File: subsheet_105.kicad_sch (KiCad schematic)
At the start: 0 parts

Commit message: prepare feuille circuit video
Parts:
- added B03: Sortie vidéo, symbol Connector_Generic:Conn_01x09
- added C? (x3): 47nF, symbol Device:C_Small
- added C?: 100uF, symbol Device:C_Polarized_Small
- added C?: 10nF, symbol Device:C_Small
- added D?: 1N4148, symbol Device:D_Small
- added I06, I10: 74LS173 Registre D 4 bits, Package_DIP:DIP-16_W7.62mm_LongPads, symbol 74x173:4-BIT_D-TYPE_REGISTERS_WITH_3-STATE_OUTPUTS_PHY
- added I18: 74LS165 Sérialiseur 8:1, Package_DIP:DIP-16_W7.62mm_LongPads, symbol 74x165:PARALLEL-LOAD_8-BIT_SHIFT_REGISTERS_PHY
- added I25: 74LS126 Quadruple tampon de bus, Package_DIP:DIP-14_W7.62mm_LongPads, symbol 74x126:QUADRUPLE_BUS_BUFFERS_WITH_3-STATE_OUTPUTS_PHY
- added R?: 22K, symbol Device:R_Small
- added R?: 3K3, symbol Device:R_Small
- added T01, T02, T03: BC547B, symbol Device:Q_NPN_EBC
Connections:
- new net +5V: C?.1, C?.2
- new net GND: C?.1, C?.2

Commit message: continue circuit vidéo
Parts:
- added C22, C26, C30, C32, C36: 47nF, symbol Device:C_Small
- added C59: 18pF, symbol Device:C_Small
- added D04, D05, D06: 1N4148, symbol Device:D_Small
- added I03: HM7603 32×8 PROM, Package_DIP:DIP-16_W7.62mm_LongPads, symbol hm7603:HM7603_32×8_PROM_THREE-STATE_OUTPUTS_PHY
- added R01, R03, R05: 1K, symbol Device:R_Small
- added R02, R04, R06: 68, symbol Device:R_Small
- added R14, R17, R20: 10K, symbol Device:R_Small
- added R15, R18, R21: 3K, symbol Device:R_Small
- added R16, R19, R22: 22K, symbol Device:R_Small
- added R23, R24, R25, R26, R27, R28: 4K7, symbol Device:R_Small
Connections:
- net +5V: now also I06.16 (VCC), I10.16 (VCC), I18.16 (VCC), I25.14 (VCC), T01.3 (C), T02.3 (C), T03.3 (C), C22.1, C26.1, C30.1, C32.1, C36.2, I03.16 (VCC), R23.1, R24.1, R25.1, R26.1, R27.1, R28.1
- net GND: now also B03.6 (Pin_6), I06.10 (~{G2}), I06.15 (CLR), I06.8 (GND), I06.9 (~{G1}), I10.10 (~{G2}), I10.15 (CLR), I10.8 (GND), I10.9 (~{G1}), I18.15 (CLK_INH), I25.7 (GND), C22.2, C26.2, C30.2, C32.2, C36.1, I03.15 (~{CE}), I03.8 (GND), R01.2, R03.2, R05.2, R14.2, R17.2, R20.2
- net at T01.1 (E): now also R01.1, R02.2
- net at T01.2 (B): now also R14.1, R15.1, R16.1
- net ~{INILT}: now reaches I25.1 (1G)
- net ~{INILT}: now also I06.2 (~{OE2}), I10.2 (~{OE2}), I25.10 (3G), I25.13 (4G), I25.4 (2G)
- net ROUGE: now reaches I25.11 (4Y)
- net ROUGE: now also I06.6 (4Q), I10.6 (4Q), I03.10 (A0)
- net RT: now reaches I25.12 (4A)
- net PT: now reaches I25.2 (1A)
- net PASTEL: now reaches I25.3 (1Y)
- net PASTEL: now also I06.3 (1Q), I10.3 (1Q), I03.13 (A3)
- net BT: now reaches I25.5 (2A)
- net BLEU: now reaches I25.6 (2Y)
- net BLEU: now also I06.4 (2Q), I10.4 (2Q), I03.12 (A2)
- net VERT: now reaches I25.8 (3Y)
- net VERT: now also I06.5 (3Q), I10.5 (3Q), I03.11 (A1)
- net VT: now reaches I25.9 (3A)
- net at I06.1 (~{OE1}): now also I18.7 (~{QH})
- net at T03.1 (E): now also R05.1, R06.2
- net at T03.2 (B): now also R20.1, R21.1, R22.1
- net at I18.9 (QH): now also I10.1 (~{OE1})
- net at T02.1 (E): now also R03.1, R04.2
- net at T02.2 (B): now also R17.1, R18.1, R19.1
- net N/SON TV: now reaches B03.1 (Pin_1)
- net B: now reaches B03.2 (Pin_2)
- net B: now also R02.1
- net R: now reaches B03.3 (Pin_3)
- net R: now also R06.1
- net CRTV: now reaches B03.4 (Pin_4)
- net F/VIDEO: now reaches B03.5 (Pin_5)
- net V: now reaches B03.7 (Pin_7)
- net V: now also R04.1
- net SYNTV: now reaches B03.8 (Pin_8)
- net CLTV: now reaches B03.9 (Pin_9)
- new net: I03.1 (O1), R22.2, R23.2
- new net: D04.2 (A), I03.2 (O2), R24.2
- new net: I03.3 (O3), R19.2, R25.2
- new net: C59.2, D05.2 (A), I03.4 (O4), R26.2
- new net: I03.5 (O5), R16.2, R27.2
- new net: D06.2 (A), I03.6 (O6), R28.2
- new net: C59.1, D05.1 (K), R18.2
- new net: D04.1 (K), R21.2
- new net: D06.1 (K), R15.2
- new net ~{NOIR_INCR}: I03.9 (O8)
- new net ~{SUPLT}: I03.14 (A4)
- no-connect marks 0 -> 1
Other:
- moved on the sheet: I06, I10, I18, I25, T01, T02, T03

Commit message: continue le circuit vidéo
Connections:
- net GND: now also I18.8 (GND)
- net DC4: now reaches I06.11 (4D)
- net DC5: now reaches I06.12 (3D)
- net DC6: now reaches I06.13 (2D)
- net DC7: now reaches I06.14 (1D)
- net ~{DATA_VALID}: now reaches I18.1 (SH/~{LD})
- net DP0: now reaches I18.11 (A)
- net DP1: now reaches I18.12 (B)
- net DP2: now reaches I18.13 (C)
- net DP3: now reaches I18.14 (D)
- net DP4: now reaches I18.3 (E)
- net DP5: now reaches I18.4 (F)
- net DP6: now reaches I18.5 (G)
- net DP7: now reaches I18.6 (H)
- net DC0: now reaches I10.11 (4D)
- net DC1: now reaches I10.12 (3D)
- net DC2: now reaches I10.13 (2D)
- net DC3: now reaches I10.14 (1D)
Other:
- moved on the sheet: C22

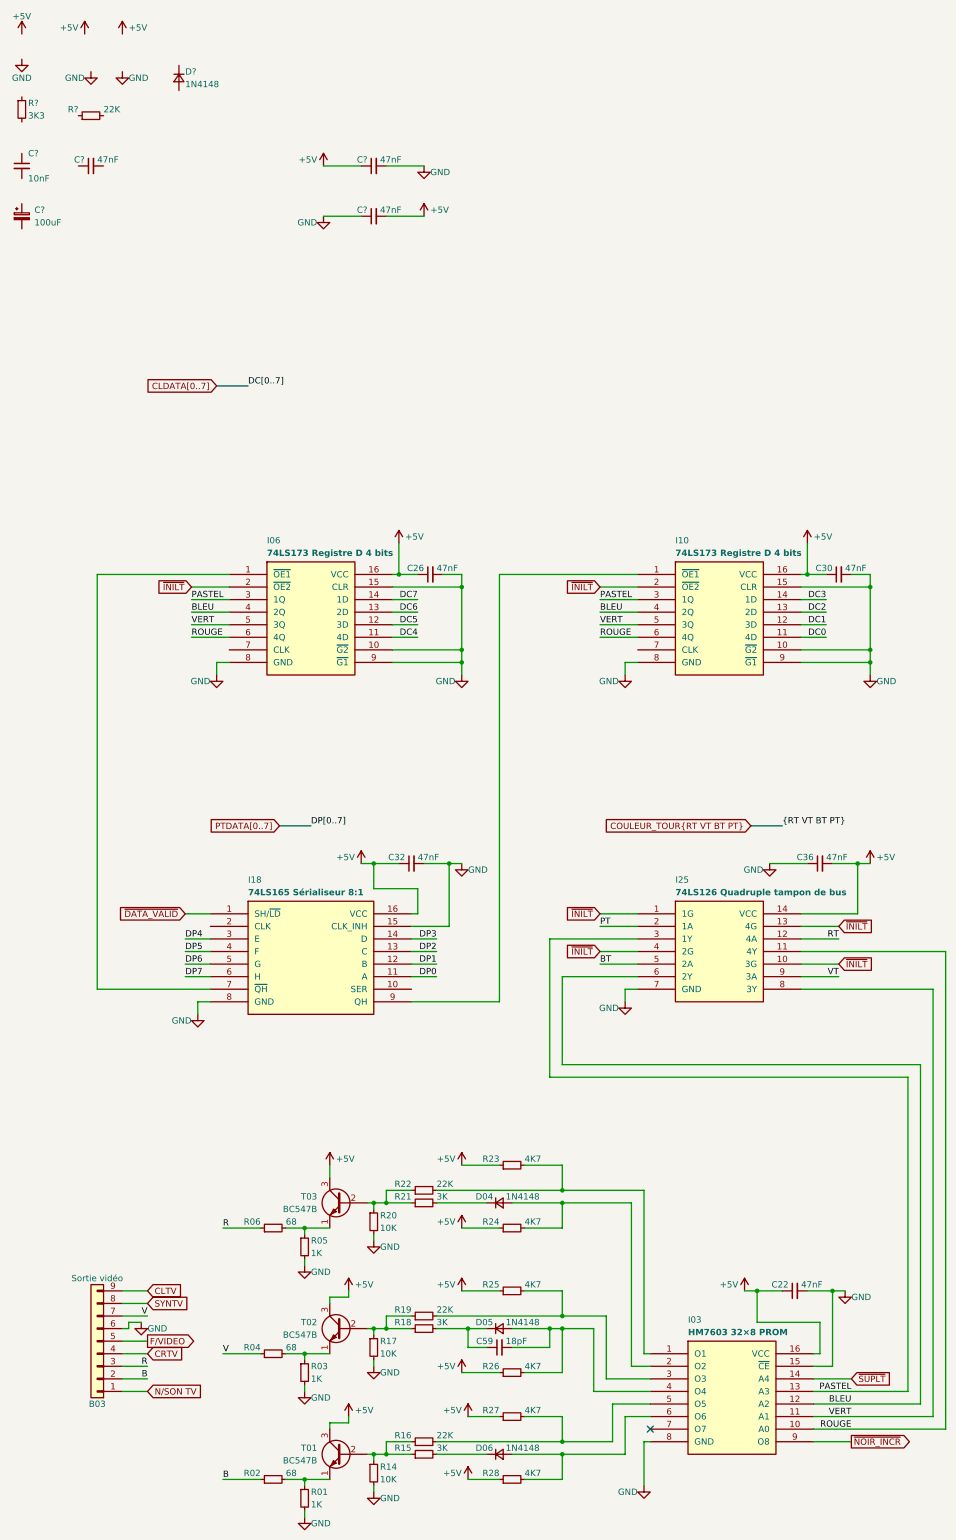
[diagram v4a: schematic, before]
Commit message: rearrange la feuille de cadencement
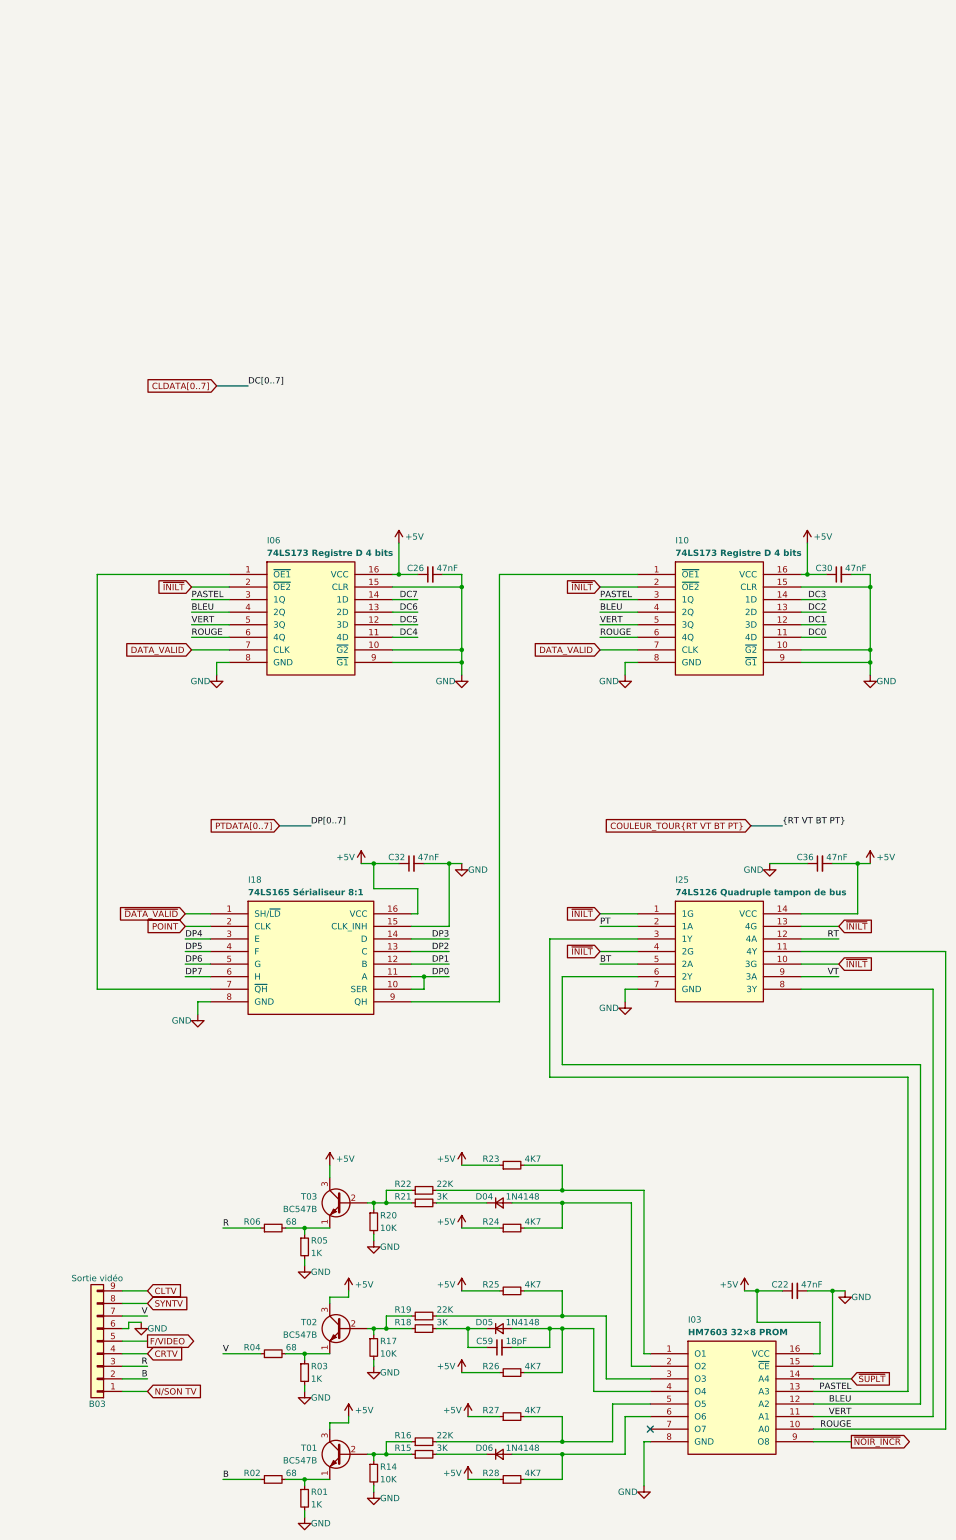
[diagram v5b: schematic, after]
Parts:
- removed C? (x3): 47nF, symbol Device:C_Small
- removed C?: 100uF, symbol Device:C_Polarized_Small
- removed C?: 10nF, symbol Device:C_Small
- removed D?: 1N4148, symbol Device:D_Small
- removed R?: 22K, symbol Device:R_Small
- removed R?: 3K3, symbol Device:R_Small
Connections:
- net DP0: now also I18.10 (SER)
- net DATA_VALID: now reaches I06.7 (CLK)
- net DATA_VALID: now also I10.7 (CLK)
- net POINT: now reaches I18.2 (CLK)
